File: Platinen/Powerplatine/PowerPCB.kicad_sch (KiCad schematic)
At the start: 35 parts, among them J1 Eingangsbuchse, J2 Conn_01x03_Pin, J3 Conn_01x03_Pin, J4 Conn_01x03_Socket, J5 Conn_01x03_Socket, U1 Generic DCDC, X1 Conn_01x03_Pin, X10 Conn_01x03_Pin, X11 Conn_01x03_Pin, X12 Conn_01x03_Pin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

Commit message: added letter matrix pdf v1
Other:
- moved on the sheet: H1, H2, H3, H4, H5
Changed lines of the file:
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@@
 	(symbol
 		(lib_id "Mechanical:MountingHole")
-		(at 173.99 71.12 0)
+		(at 185.42 63.5 0)
 		(unit 1)
 		(exclude_from_sim yes)
@@
 		(dnp no)
 		(property "Reference" "H4"
-			(at 176.53 69.8499 0)
+			(at 187.96 62.2299 0)
 			(effects
 				(font
@@
 		)
 		(property "Value" "MountingHole"
-			(at 176.53 72.3899 0)
+			(at 187.96 64.7699 0)
 			(effects
 				(font
@@
 		)
 		(property "Footprint" "MountingHole:MountingHole_3.2mm_M3_DIN965"
-			(at 173.99 71.12 0)
-			(effects
-				(font
-					(size 1.27 1.27)
-				)
-				(hide yes)
-			)
-		)
-		(property "Datasheet" "~"
-			(at 173.99 71.12 0)
+			(at 185.42 63.5 0)
+			(effects
+				(font
+					(size 1.27 1.27)
+				)
+				(hide yes)
+			)
+		)
+		(property "Datasheet" "~"
+			(at 185.42 63.5 0)
 			(effects
 				(font
@@
 		)
 		(property "Description" "Mounting Hole without connection"
-			(at 173.99 71.12 0)
+			(at 185.42 63.5 0)
 			(effects
 				(font
@@
 	(symbol
 		(lib_id "Mechanical:MountingHole")
-		(at 182.88 71.12 0)
+		(at 194.31 63.5 0)
 		(unit 1)
 		(exclude_from_sim yes)
@@
 		(fields_autoplaced yes)
 		(property "Reference" "H5"
-			(at 185.42 69.8499 0)
+			(at 196.85 62.2299 0)
 			(effects
 				(font
@@
 		)
 		(property "Value" "MountingHole"
-			(at 185.42 72.3899 0)
+			(at 196.85 64.7699 0)
 			(effects
 				(font
@@
 		)
 		(property "Footprint" "MountingHole:MountingHole_3.2mm_M3_DIN965"
-			(at 182.88 71.12 0)
-			(effects
-				(font
-					(size 1.27 1.27)
-				)
-				(hide yes)
-			)
-		)
-		(property "Datasheet" "~"
-			(at 182.88 71.12 0)
+			(at 194.31 63.5 0)
+			(effects
+				(font
+					(size 1.27 1.27)
+				)
+				(hide yes)
+			)
+		)
+		(property "Datasheet" "~"
+			(at 194.31 63.5 0)
 			(effects
 				(font
@@
 		)
 		(property "Description" "Mounting Hole without connection"
-			(at 182.88 71.12 0)
+			(at 194.31 63.5 0)
 			(effects
 				(font
@@
 	(symbol
 		(lib_id "Mechanical:MountingHole")
-		(at 165.1 71.12 0)
+		(at 176.53 63.5 0)
 		(unit 1)
 		(exclude_from_sim yes)
@@
 		(fields_autoplaced yes)
 		(property "Reference" "H3"
-			(at 167.64 69.8499 0)
+			(at 179.07 62.2299 0)
 			(effects
 				(font
@@
 		)
 		(property "Value" "MountingHole"
-			(at 167.64 72.3899 0)
+			(at 179.07 64.7699 0)
 			(effects
 				(font
@@
 		)
 		(property "Footprint" "MountingHole:MountingHole_3.2mm_M3_DIN965"
-			(at 165.1 71.12 0)
-			(effects
-				(font
-					(size 1.27 1.27)
-				)
-				(hide yes)
-			)
-		)
-		(property "Datasheet" "~"
-			(at 165.1 71.12 0)
+			(at 176.53 63.5 0)
+			(effects
+				(font
+					(size 1.27 1.27)
+				)
+				(hide yes)
+			)
+		)
+		(property "Datasheet" "~"
+			(at 176.53 63.5 0)
 			(effects
 				(font
@@
 		)
 		(property "Description" "Mounting Hole without connection"
-			(at 165.1 71.12 0)
+			(at 176.53 63.5 0)
 			(effects
 				(font
@@
 	(symbol
 		(lib_id "Mechanical:MountingHole")
-		(at 156.21 71.12 0)
+		(at 167.64 63.5 0)
 		(unit 1)
 		(exclude_from_sim yes)
@@
 		(fields_autoplaced yes)
 		(property "Reference" "H2"
-			(at 158.75 69.8499 0)
+			(at 170.18 62.2299 0)
 			(effects
 				(font
@@
 		)
 		(property "Value" "MountingHole"
-			(at 158.75 72.3899 0)
+			(at 170.18 64.7699 0)
 			(effects
 				(font
@@
 		)
 		(property "Footprint" "MountingHole:MountingHole_3.2mm_M3_DIN965"
-			(at 156.21 71.12 0)
-			(effects
-				(font
-					(size 1.27 1.27)
-				)
-				(hide yes)
-			)
-		)
-		(property "Datasheet" "~"
-			(at 156.21 71.12 0)
+			(at 167.64 63.5 0)
+			(effects
+				(font
+					(size 1.27 1.27)
+				)
+				(hide yes)
+			)
+		)
+		(property "Datasheet" "~"
+			(at 167.64 63.5 0)
 			(effects
 				(font
@@
 		)
 		(property "Description" "Mounting Hole without connection"
-			(at 156.21 71.12 0)
+			(at 167.64 63.5 0)
 			(effects
 				(font
@@
 	(symbol
 		(lib_id "Mechanical:MountingHole")
-		(at 147.32 71.12 0)
+		(at 158.75 63.5 0)
 		(unit 1)
 		(exclude_from_sim yes)
@@
 		(fields_autoplaced yes)
 		(property "Reference" "H1"
-			(at 149.86 69.8499 0)
+			(at 161.29 62.2299 0)
 			(effects
 				(font
@@
 		)
 		(property "Value" "MountingHole"
-			(at 149.86 72.3899 0)
+			(at 161.29 64.7699 0)
 			(effects
 				(font
@@
 		)
 		(property "Footprint" "MountingHole:MountingHole_3.2mm_M3_DIN965"
-			(at 147.32 71.12 0)
-			(effects
-				(font
-					(size 1.27 1.27)
-				)
-				(hide yes)
-			)
-		)
-		(property "Datasheet" "~"
-			(at 147.32 71.12 0)
+			(at 158.75 63.5 0)
+			(effects
+				(font
+					(size 1.27 1.27)
+				)
+				(hide yes)
+			)
+		)
+		(property "Datasheet" "~"
+			(at 158.75 63.5 0)
 			(effects
 				(font
@@
 		)
 		(property "Description" "Mounting Hole without connection"
-			(at 147.32 71.12 0)
-			(effects
-				(font
+			(at 158.75 63.5 0)
+			(effects
+				(font

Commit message: Adjusted letter matrix and added stencil verśion
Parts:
- added FID1, FID2, FID3: Fiducial, Fiducial:Fiducial_1.5mm_Mask3mm, symbol Mechanical:Fiducial
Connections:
- net at X10.2 (Pin_2): now also X11.2 (Pin_2); no longer X9.2 (Pin_2)
- net at J5.2 (Pin_2): no longer X14.2 (Pin_2)
- net at J4.2 (Pin_2), X7.2 (Pin_2): no longer X8.2 (Pin_2)
- net at J2.2 (Pin_2), X6.2 (Pin_2): no longer X5.2 (Pin_2)
- net at X12.2 (Pin_2): now also X13.2 (Pin_2); no longer X11.2 (Pin_2)
- net at X2.2 (Pin_2): now also X3.2 (Pin_2); no longer X1.2 (Pin_2)
- net at X19.2 (Pin_2): now also X18.2 (Pin_2)
- net at X15.2 (Pin_2): now also X14.2 (Pin_2); no longer X16.2 (Pin_2)
- net at J3.2 (Pin_2): no longer X13.2 (Pin_2)
- net at X4.2 (Pin_2): now also X5.2 (Pin_2); no longer X3.2 (Pin_2)
- net at X17.2 (Pin_2): now also X16.2 (Pin_2); no longer X18.2 (Pin_2)
- new net: X8.2 (Pin_2), X9.2 (Pin_2)
- no-connect marks 1 -> 2

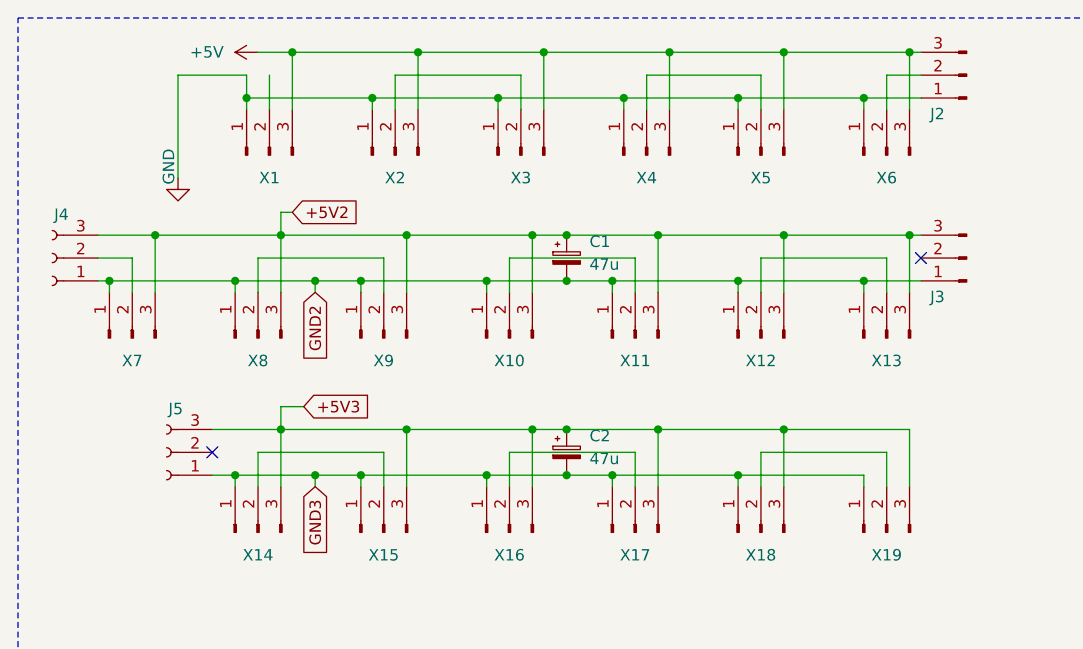
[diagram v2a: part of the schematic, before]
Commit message: added trotec template
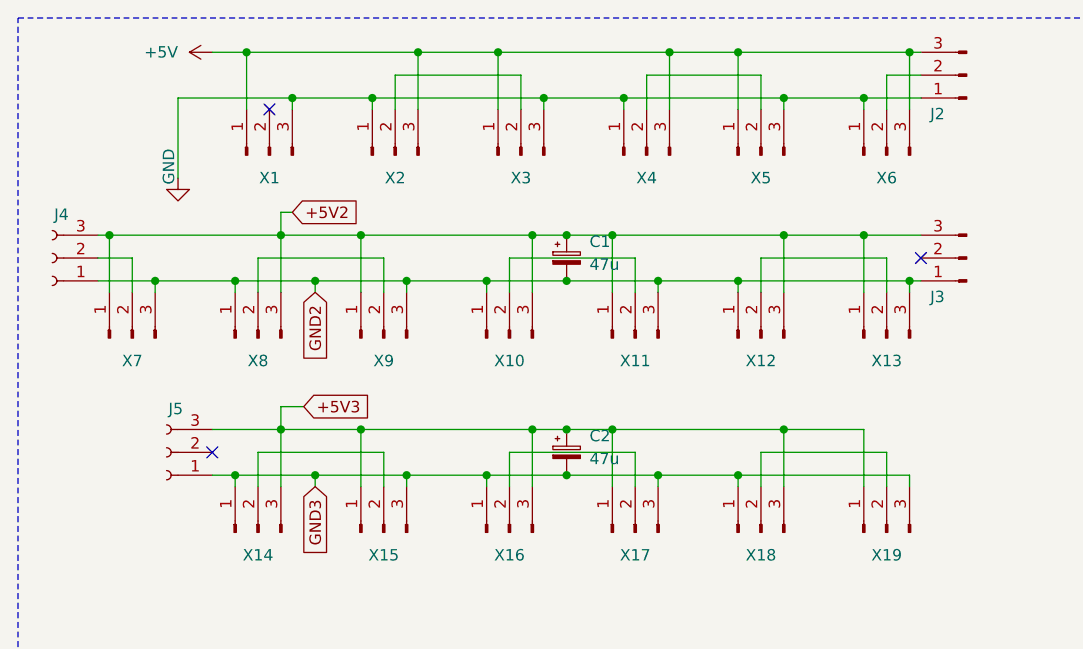
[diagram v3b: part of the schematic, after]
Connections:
- net +5V: now also X1.1 (Pin_1), X3.1 (Pin_1), X5.1 (Pin_1); no longer X1.3 (Pin_3), X3.3 (Pin_3), X5.3 (Pin_3)
- net +5V2: now also X11.1 (Pin_1), X13.1 (Pin_1), X7.1 (Pin_1), X9.1 (Pin_1); no longer X11.3 (Pin_3), X13.3 (Pin_3), X7.3 (Pin_3), X9.3 (Pin_3)
- net +5V3: now also X15.1 (Pin_1), X17.1 (Pin_1), X19.1 (Pin_1); no longer X15.3 (Pin_3), X17.3 (Pin_3), X19.3 (Pin_3)
- net GND: now also X1.3 (Pin_3), X3.3 (Pin_3), X5.3 (Pin_3); no longer X1.1 (Pin_1), X3.1 (Pin_1), X5.1 (Pin_1)
- net GND2: now also X11.3 (Pin_3), X13.3 (Pin_3), X7.3 (Pin_3), X9.3 (Pin_3); no longer X11.1 (Pin_1), X13.1 (Pin_1), X7.1 (Pin_1), X9.1 (Pin_1)
- net GND3: now also X15.3 (Pin_3), X17.3 (Pin_3), X19.3 (Pin_3); no longer X15.1 (Pin_1), X17.1 (Pin_1), X19.1 (Pin_1)
- no-connect marks 2 -> 3
